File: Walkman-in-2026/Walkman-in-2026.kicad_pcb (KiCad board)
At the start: 2 copper layers, 100 x 63.5 mm, 36 parts, among them J1 AudioJack3, J2 Micro_SD_Card, Q1 BSS138, Q2 BSS138, SW1 SW_Push, SW2 SW_Push, SW3 SW_Push, SW4 SW_SPST, SW5 SW_Push, SW6 SW_Push, U1 XIAO-ESP32-S3-DIP, U2 HS1602A-B, U3 PCM5102, U4 PCF8574P

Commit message: adding a fking stupid battery
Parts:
- added J3: Conn_01x02_Socket, Connector_Molex:Molex_KK-254_AE-6410-02A_1x02_P2.54mm_Vertical, F.Cu at (257.5, 97.0)
- moved SW4 4.00 mm to (254.0, 86.5)
- moved SW1 0.75 mm to (217.8, 82.2)
- moved SW2 0.75 mm to (226.3, 82.2)
- moved SW3 0.75 mm to (234.8, 82.2)
- moved SW5 0.75 mm to (243.4, 82.2)
- moved SW6 0.75 mm to (251.9, 82.2)
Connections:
- SW4 pad 2: +3.3V -> Net-(BT1--)
- U1 pad 12: Net-(SW4-A) -> +3.3V
- U1 pad 14: +5V -> Net-(SW4-A)
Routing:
- net +3.3V: track 142.7 -> 98.9 mm, vias 3 -> 1
- net +5V: track 112.7 -> 81.4 mm
- net unconnected-(J2-SHIELD-PadSH)_3: track 30.8 -> 0.00 mm
- net Net-(U1-GPIO1_A0_D0): track 176.7 -> 189.7 mm
- net GND: track 300.6 -> 312.0 mm
- net Net-(SW4-A): track 91.3 -> 99.8 mm
- net Net-(R2-Pad1): track 21.2 -> 22.1 mm
- net +3V3: track 120.4 -> 121.1 mm

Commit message: larp
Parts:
- removed C1, C2: 2.2, Capacitor_THT:C_Disc_D3.0mm_W1.6mm_P2.50mm
- removed C10: 10, Capacitor_THT:C_Radial_D5.0mm_H5.0mm_P2.00mm
- removed C3, C5: 2.2, Capacitor_THT:C_Radial_D5.0mm_H5.0mm_P2.00mm
- removed C6, C7, C8: 0.1, Capacitor_THT:C_Disc_D3.0mm_W1.6mm_P2.50mm
- removed C9: 0.1, Capacitor_THT:C_Radial_D5.0mm_H5.0mm_P2.00mm
- removed J3: Conn_01x02_Socket, Connector_Molex:Molex_KK-254_AE-6410-02A_1x02_P2.54mm_Vertical
- removed R12, R13: 470, Resistor_THT:R_Axial_DIN0207_L6.3mm_D2.5mm_P7.62mm_Horizontal
- removed U3: PCM5102, Package_SO:TSSOP-20_4.4x6.5mm_P0.65mm
- added JP1: Jumper_2_Bridged, TestPoint:TestPoint_2Pads_Pitch2.54mm_Drill0.8mm, F.Cu at (254.5, 111.8)
- added U5: ~, Connector_PinHeader_2.54mm:PinHeader_1x15_P2.54mm_Vertical, F.Cu at (185.5, 112.0)
- J1: value AudioJack3 -> Conn_01x01_Pin; footprint Connector_Audio:Jack_3.5mm_CUI_SJ1-3513N_Horizontal -> Connector_PinHeader_1.00mm:PinHeader_1x01_P1.00mm_Vertical
- R2: value 1k -> 10k
- R4: value 1k -> 4.7k
- R5: value 1k -> 22k
- R6: value 1k -> 47k
- SW1, SW2, SW3, SW5, SW6: footprint Button_Switch_THT:SW_PUSH_6mm -> easyeda2kicad:SW-SMD_TC-S3601-3.5-260G-F0.6
- moved SW1 49.5 mm to (203.3, 129.6), turned to 180 degrees
- moved SW2 49.2 mm to (212.8, 129.6), turned to 180 degrees
- moved SW3 49.0 mm to (222.3, 129.6), turned to 180 degrees
- moved SW5 48.7 mm to (232.2, 129.6), turned to 180 degrees
- moved SW6 48.5 mm to (241.7, 129.6), turned to 180 degrees
- moved J1 44.0 mm to (200.7, 123.0), turned to 0 degrees
- moved R7 43.5 mm to (167.7, 82.2), turned to -90 degrees
- moved J2 41.2 mm to (191.0, 122.5), turned to 180 degrees
- moved R9 35.8 mm to (164.0, 89.8)
- moved R10 35.5 mm to (167.5, 92.5)
- moved R8 35.5 mm to (164.0, 100.0)
- moved U1 35.4 mm to (173.0, 120.9), turned to -90 degrees
- moved R11 33.9 mm to (178.3, 79.5), turned to 180 degrees
- moved R1 32.5 mm to (170.7, 76.0)
- moved SW4 31.5 mm to (254.5, 118.0)
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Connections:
- R10 pad 2: +5V -> VBUS
- R2 pad 1: Net-(R2-Pad1) -> GPIO1
- R3 pad 1: Net-(R3-Pad1) -> GPIO1
- R3 pad 2: Net-(R2-Pad1) -> Net-(R3-Pad2)
- R4 pad 2: Net-(R3-Pad1) -> GPIO1
- R5 pad 1: Net-(R5-Pad1) -> GPIO1
- R5 pad 2: Net-(R4-Pad1) -> Net-(R5-Pad2)
- R6 pad 1: GND -> GPIO1
- R6 pad 2: Net-(R5-Pad1) -> Net-(R6-Pad2)
- R7 pad 2: +5V -> VBUS
- SW1 pad 1: Net-(U1-GPIO1_A0_D0) -> GND
- SW1 pad 2: +3V3 -> GPIO1
- SW2 pad 1: Net-(U1-GPIO1_A0_D0) -> GND
- SW2 pad 2: Net-(R2-Pad1) -> Net-(R3-Pad2)
- SW3 pad 1: Net-(U1-GPIO1_A0_D0) -> GND
- SW3 pad 2: Net-(R3-Pad1) -> Net-(R4-Pad1)
- SW4 pad 1: Net-(SW4-A) -> Net-(J1-Pin_1)
- SW5 pad 1: Net-(U1-GPIO1_A0_D0) -> GND
- SW5 pad 2: Net-(R4-Pad1) -> Net-(R5-Pad2)
- SW6 pad 1: Net-(U1-GPIO1_A0_D0) -> GND
- SW6 pad 2: Net-(R5-Pad1) -> Net-(R6-Pad2)
- U1 pad 1: Net-(U1-GPIO1_A0_D0) -> GPIO1
- U1 pad 14: Net-(SW4-A) -> VBUS
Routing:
- net GPIO1: track 0.00 -> 210.9 mm
- net Net-(U1-GPIO1_A0_D0): track 189.7 -> 0.00 mm
- net +3V3: track 121.1 -> 13.4 mm, vias 1 -> 0
- net Net-(SW4-A): track 99.8 -> 0.00 mm
- net VBUS: track 0.00 -> 80.1 mm
- net Net-(J1-Pin_1): track 0.00 -> 55.9 mm
- net Net-(U3-OUTR): track 55.2 -> 0.00 mm, vias 1 -> 0
- net GND: track 312.0 -> 258.1 mm, vias 5 -> 0
- net Net-(U3-OUTL): track 50.4 -> 0.00 mm, vias 1 -> 0
- net Net-(J2-DAT3/CD): track 62.1 -> 13.9 mm
- net Net-(U1-GPIO44_D7_RX): track 23.2 -> 67.4 mm, vias 1 -> 0
- net Net-(U2-RS): track 40.0 -> 80.1 mm
- net Net-(C1-Pad2): track 32.7 -> 0.00 mm, vias 2 -> 0
- net Net-(C2-Pad2): track 29.5 -> 0.00 mm
- net Net-(U2-E): track 44.6 -> 72.2 mm
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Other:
- board size 100 x 63.5 mm -> 99 x 60 mm
- board text added: "BAT+"
- board text added: "CADed and assembled by Brandon Kim (BK)"
- board text added: "GND"
- board text added: "Makoto's Walkman (P3) V1"

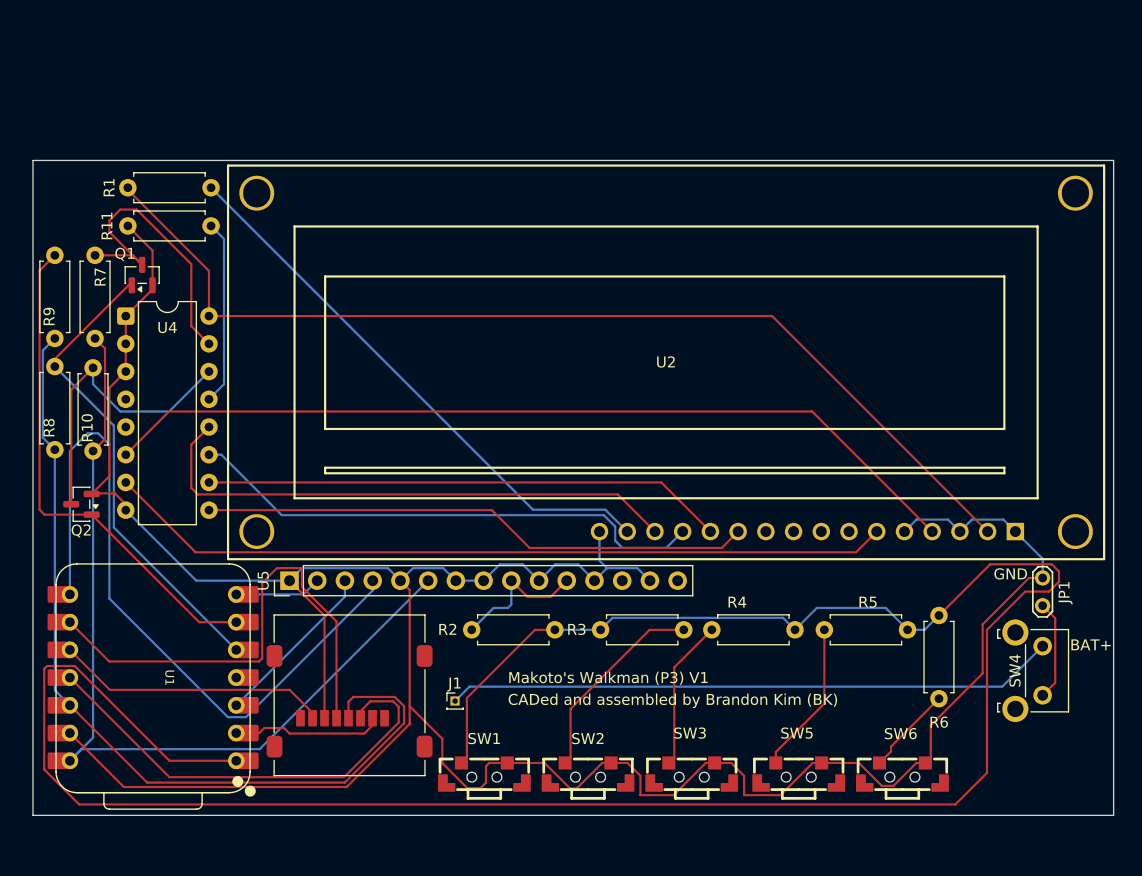
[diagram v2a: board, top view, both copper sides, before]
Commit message: Adding custom footprints for lcd x pcf and pcm x audiojack
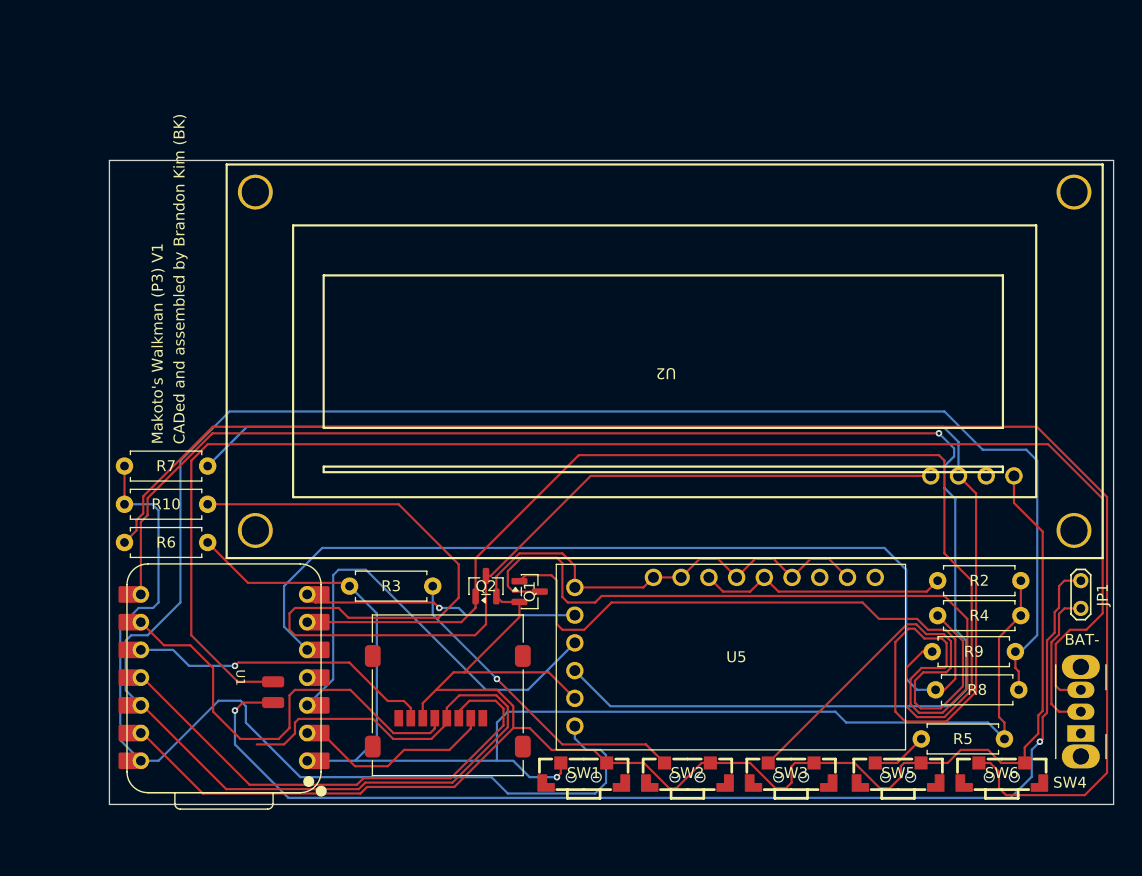
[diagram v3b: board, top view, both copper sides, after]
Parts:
- removed J1: Conn_01x01_Pin, Connector_PinHeader_1.00mm:PinHeader_1x01_P1.00mm_Vertical
- removed R1: 33, Resistor_THT:R_Axial_DIN0207_L6.3mm_D2.5mm_P7.62mm_Horizontal
- removed R11: 10k, Resistor_THT:R_Axial_DIN0207_L6.3mm_D2.5mm_P7.62mm_Horizontal
- removed U4: PCF8574P, Package_DIP:DIP-16_W7.62mm
- JP1: value Jumper_2_Bridged -> Jumper_2_Open
- SW4: value SW_SPST -> SW_SPDT; footprint Button_Switch_THT:SW_SPST_Omron_B3F-315x_Angled -> Button_Switch_THT:SW_Slide_SPDT_Angled_CK_OS102011MA1Q
- U2: value HS1602A-B -> ~; footprint EasyEDALibrary:LCD1602 -> PCF x LCD combo:PCF8574 x LCD1602 combo
- U5: footprint Connector_PinHeader_2.54mm:PinHeader_1x15_P2.54mm_Vertical -> Amazon_PCM:PCM x AudioJack Combo
- moved R9 92.6 mm to (252.0, 118.5), turned to 180 degrees
- moved R8 91.0 mm to (252.3, 122.0), turned to 180 degrees
- moved R6 67.3 mm to (178.0, 108.5), turned to 180 degrees
- moved Q1 45.8 mm to (207.5, 113.0), turned to 0 degrees
- moved R2 42.9 mm to (252.5, 112.0)
- moved U5 41.0 mm to (225.9, 119.0), turned to 0 degrees
- moved Q2 37.8 mm to (203.5, 112.5), turned to 90 degrees
- moved R3 23.3 mm to (191.0, 112.5)
- moved R7 21.9 mm to (178.0, 101.5), turned to 180 degrees
- moved R4 20.7 mm to (244.9, 115.2)
- moved R10 16.3 mm to (178.0, 105.0), turned to 180 degrees
- moved R5 13.4 mm to (251.0, 126.5)
- moved SW1 9.11 mm to (212.5, 129.6)
- moved SW2 9.11 mm to (222.0, 129.6)
- moved SW3 9.11 mm to (231.5, 129.6)
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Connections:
- net Net-(JP1-B) renamed +BATT
- JP1 pad 1: GND -> BATT-
- SW4 pad 1: Net-(J1-Pin_1) -> unconnected-(SW4-A-Pad1)
- U2 pad 0: unconnected-(U2-EH-Pad0)_3 -> (no net)
- U2 pad 3: GND -> Net-(Q1-D)
- U2 pad 4: Net-(U2-RS) -> Net-(Q2-D)
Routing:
- net Net-(Q1-D): track 27.9 -> 188.3 mm
- net BATT+: track 0.00 -> 133.7 mm
- net Net-(R6-Pad2): track 8.15 -> 138.5 mm
- net +3.3V: track 79.6 -> 199.6 mm
- net BATT-: track 0.00 -> 103.6 mm, vias 0 -> 2
- net +5V: track 94.4 -> 0.00 mm
- net Net-(Q1-G): track 43.4 -> 132.0 mm
- net Net-(Q2-D): track 28.0 -> 114.3 mm
- net GPIO1: track 210.9 -> 124.9 mm, vias 0 -> 1
- net Net-(U2-RS): track 80.1 -> 0.00 mm
- net Net-(U1-GPIO44_D7_RX): track 67.4 -> 147.1 mm, vias 0 -> 1
- net Net-(U2-E): track 72.2 -> 0.00 mm
- net Net-(Q2-G): track 46.2 -> 103.6 mm
- net Net-(J1-Pin_1): track 55.9 -> 0.00 mm
- net GND: track 258.1 -> 203.2 mm
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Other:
- board size 99 x 60 mm -> 92 x 59 mm
- board text added: "BAT-"
- board text removed: "BAT+"
- board text removed: "GND"

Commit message: v1 final
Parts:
- moved U2 1.60 mm to (221.2, 91.0)
- moved Q2 1.50 mm to (202.0, 112.5), turned to -90 degrees
- moved Q1 0.50 mm to (207.5, 112.5)
- moved R3 0.50 mm to (190.5, 112.5)
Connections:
- net Net-(J2-CLK) renamed SCK
- net Net-(J2-CMD) renamed MOSI
- net Net-(J2-DAT0) renamed MISO
- net Net-(J2-DAT3/CD) renamed DAT3
- net Net-(U1-GPIO3_A2_D2) renamed AJDIN
- net Net-(U1-GPIO43_D6_TX) renamed AJBCK
- net Net-(U1-GPIO44_D7_RX) renamed AJLCK
- Q1 pad 1: Net-(Q1-G) -> +3.3V
- Q1 pad 2: GND -> SDA
- Q2 pad 1: Net-(Q2-G) -> +3.3V
- Q2 pad 2: GND -> SCL
- R8 pad 2: Net-(Q1-G) -> SDA
- R9 pad 2: Net-(Q2-G) -> SCL
- U1 pad 5: Net-(Q1-G) -> SDA
- U1 pad 6: Net-(Q2-G) -> SCL
- U2 pad 2: +5V -> VBUS
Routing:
- net Net-(Q1-G): track 132.0 -> 0.00 mm
- net Net-(Q1-D): track 188.3 -> 57.4 mm
- net Net-(Q2-G): track 103.6 -> 0.00 mm
- net SDA: track 0.00 -> 103.2 mm
- net SCL: track 0.00 -> 90.6 mm
- net Net-(Q2-D): track 114.3 -> 45.3 mm
- net BATT+: track 133.7 -> 175.2 mm
- net VBUS: track 89.6 -> 117.1 mm
- net Net-(R6-Pad2): track 138.5 -> 165.0 mm
- net AJLCK: track 147.1 -> 168.6 mm
- net Net-(R4-Pad1): track 43.8 -> 28.5 mm
- net Net-(R3-Pad2): track 29.5 -> 37.4 mm
- net AJDIN: track 41.6 -> 49.4 mm
- net +3.3V: track 199.6 -> 205.8 mm, vias 0 -> 2
- net GND: track 203.2 -> 205.8 mm
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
